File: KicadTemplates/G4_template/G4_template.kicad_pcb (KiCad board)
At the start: 2 copper layers, 71.1 x 83.2 mm, 10 parts, among them J1 Conn_01x04_Female, J2 Conn_01x03_Male, J3 Conn_01x03_Male, J4 Conn_02x10_Odd_Even, J5 Conn_02x03_Odd_Even, J6 Conn_01x01_Female, SW1 SW_SPDT, U2 NUCLEO-G491RE

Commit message: updated template
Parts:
- removed U2: NUCLEO-G491RE, G4Lib:MODULE_NUCLEO-G491RE
- added J_PWR1: Conn_01x05_Female, Connector_JST:JST_XH_S5B-XH-A_1x05_P2.50mm_Horizontal, F.Cu at (118.7, 59.1)
- added R1: 4.4K, Resistor_THT:R_Axial_DIN0207_L6.3mm_D2.5mm_P7.62mm_Horizontal, F.Cu at (153.0, 66.0)
- added R2: 4.4K, Resistor_THT:R_Axial_DIN0207_L6.3mm_D2.5mm_P7.62mm_Horizontal, F.Cu at (149.0, 66.0)
- added U1: NUCLEO-G491RE, G4Lib:MODULE_NUCLEO-G491RE20, F.Cu at (127.6, 94.0)
- moved J1 25.8 mm to (161.9, 65.4)
- moved J_GND1 25.6 mm to (144.1, 130.8)
- moved J_BUS1 23.7 mm to (156.8, 59.1)
- moved J_TRACK1 23.4 mm to (96.6, 59.1)
- moved J_POW1 23.3 mm to (96.5, 59.1)
- moved J_BUS2 23.1 mm to (138.4, 59.1)
- moved SW1 22.9 mm to (99.3, 70.7)
- moved J_SRV1 22.5 mm to (116.2, 125.1)
- moved J_SRV2 22.5 mm to (129.5, 125.1)
- renumbered J6 to J_GND1, J5 to J_POW1, J2 to J_SRV1, J3 to J_SRV2, J4 to J_TRACK1
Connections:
- net Net-(J_BUS1-Pad4) renamed CANH
- net Net-(J_BUS1-Pad5) renamed CANL
- J1 pad 1: unconnected-(J1-Pad1) -> I2C3_DTA
- J1 pad 2: unconnected-(J1-Pad2) -> I2C3_CK
- J1 pad 3: unconnected-(J1-Pad3) -> 3V3
- J1 pad 4: unconnected-(J1-Pad4) -> GND
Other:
- board size 71.1 x 83.2 mm -> 71.1 x 82.5 mm
- board text added: "Template G4 V2"
- board text added: "© Daniel Braun 2024"
- board text removed: "Template G4 V1"
- board text removed: "© Daniel Braun 2023"

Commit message: update spec
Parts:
- added R3: 4.4K, Resistor_THT:R_Axial_DIN0207_L6.3mm_D2.5mm_P7.62mm_Horizontal, F.Cu at (63.5, 101.0)
- added R4: 4.4K, Resistor_THT:R_Axial_DIN0207_L6.3mm_D2.5mm_P7.62mm_Horizontal, F.Cu at (76.2, 101.6)
- moved J_GND1 56.6 mm to (161.3, 76.8)
- moved SW1 34.9 mm to (86.4, 38.2)
- moved J_SRV1 28.6 mm to (121.9, 153.1)
- moved J_SRV2 26.6 mm to (137.1, 150.6)
- moved J_POW1 17.3 mm to (98.4, 76.2), turned to 180 degrees
- moved J_TRACK1 17.2 mm to (98.4, 76.2), turned to 180 degrees
- moved J_PWR1 6.04 mm to (116.8, 53.3)
- moved J_BUS2 5.89 mm to (137.1, 53.3)
- moved J_BUS1 5.44 mm to (156.8, 53.6)
- moved J1 1.43 mm to (161.3, 64.1)
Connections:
- J1 pad 2: I2C3_CK -> I2C3_SCL
- J_POW1 pad 6: unconnected-(J_POW1-Pin_6-Pad6) -> GND
- J_TRACK1 pad 6: unconnected-(J_TRACK1-Pin_6-Pad6) -> GND
- R2 pad 1: I2C3_CK -> I2C3_SCL
- SW1 pad 3: 5VCPU -> 5VCPU_IN
- U1 pad CN10_1: unconnected-(U1B-PC9-PadCN10_1) -> I2C3_SDA
- U1 pad CN10_11: unconnected-(U1B-PA5-PadCN10_11) -> LD2
- U1 pad CN10_12: unconnected-(U1B-PA12/CAN1TX-PadCN10_12) -> CAN_TX
- U1 pad CN10_13: unconnected-(U1B-PA6-PadCN10_13) -> ADC2_IN3
- U1 pad CN10_14: unconnected-(U1B-PA11-PadCN10_14) -> CAN_RX
- U1 pad CN10_15: unconnected-(U1B-PA7-PadCN10_15) -> ADC2_IN4
- U1 pad CN10_18: (no net) -> TIM2_CH4
- U1 pad CN10_2: unconnected-(U1B-PC8-PadCN10_2) -> I2C3_SCL
- U1 pad CN10_20: unconnected-(U1B-CN10_GND-PadCN10_20) -> GND
- U1 pad CN10_21: unconnected-(U1B-PA9-PadCN10_21) -> PWM_0_1
- U1 pad CN10_22: unconnected-(U1B-PB2-PadCN10_22) -> EECS
- U1 pad CN10_23: unconnected-(U1B-PA8-PadCN10_23) -> PWM_0_0
- U1 pad CN10_24: unconnected-(U1B-PB1-PadCN10_24) -> PWM_3_1
- U1 pad CN10_25: unconnected-(U1B-PB10-PadCN10_25) -> TIM2_CH3
- U1 pad CN10_26: unconnected-(U1B-PB15-PadCN10_26) -> SPI2_MOSI
- U1 pad CN10_28: unconnected-(U1B-PB14-PadCN10_28) -> SPI2_MISO
- U1 pad CN10_3: Net-(U1B-PB8/CAN1RX) -> unconnected-(U1B-PB8/BOOT0-PadCN10_3)
- U1 pad CN10_30: unconnected-(U1B-PB13-PadCN10_30) -> SPI2_SCK
- U1 pad CN10_31: unconnected-(U1B-PB3-PadCN10_31) -> SWO
- U1 pad CN10_33: unconnected-(U1B-PA10-PadCN10_33) -> PWM_1_0
- U1 pad CN10_34: unconnected-(U1B-PC4-PadCN10_34) -> ADC2_IN5
- U1 pad CN10_4: unconnected-(U1B-PC6-PadCN10_4) -> PWM_2_0
- U1 pad CN10_5: unconnected-(U1B-PB9-PadCN10_5) -> S_IN
- U1 pad CN10_6: unconnected-(U1B-PC5-PadCN10_6) -> ASENSE
- U1 pad CN10_9: unconnected-(U1B-CN10_GND-PadCN10_9) -> GND
- U1 pad CN7_1: unconnected-(U1A-PC10/SPI3_SCK-PadCN7_1) -> SPI3_SCK
- U1 pad CN7_13: unconnected-(U1A-PA13-PadCN7_13) -> SWDIO
- U1 pad CN7_15: unconnected-(U1A-PA14-PadCN7_15) -> SWDCLK
- U1 pad CN7_17: unconnected-(U1A-PA15-PadCN7_17) -> I2C1_SCL
- U1 pad CN7_18: unconnected-(U1A-CN7_+5V-PadCN7_18) -> 5VCPU
- U1 pad CN7_2: unconnected-(U1A-PC11/SPI3_MISO-PadCN7_2) -> S_VALID
- U1 pad CN7_21: unconnected-(U1A-PB7-PadCN7_21) -> I2C1_SDA
- U1 pad CN7_28: unconnected-(U1A-PA0-PadCN7_28) -> ADC2_IN1
- U1 pad CN7_3: unconnected-(U1A-PC12/SPI3_MOSI-PadCN7_3) -> SPI3_MOSI
- U1 pad CN7_30: unconnected-(U1A-PA1-PadCN7_30) -> ADC2_IN2
- U1 pad CN7_32: unconnected-(U1A-PA4-PadCN7_32) -> PWM_2_1
- U1 pad CN7_34: unconnected-(U1A-PB0-PadCN7_34) -> PWM_3_0
- U1 pad CN7_35: unconnected-(U1A-PC2-PadCN7_35) -> ADC2_IN8
- U1 pad CN7_36: unconnected-(U1A-PC1/PB9-PadCN7_36) -> ADC2_IN7
- U1 pad CN7_37: unconnected-(U1A-PC3-PadCN7_37) -> PWM_1_1
- U1 pad CN7_38: unconnected-(U1A-PC0/PB8-PadCN7_38) -> ADC2_IN6
- U1 pad CN7_4: unconnected-(U1A-PD2-PadCN7_4) -> S_CLR
- U1 pad CN7_5: unconnected-(U1A-VDD-PadCN7_5) -> 3V3
- U1 pad CN7_6: unconnected-(U1A-E5V-PadCN7_6) -> 5VCPU_IN
- U1 pad SER0: Net-(U1B-PB8/CAN1RX) -> unconnected-(U1-PadSER0)
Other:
- board size 71.1 x 82.5 mm -> 70.5 x 91.4 mm

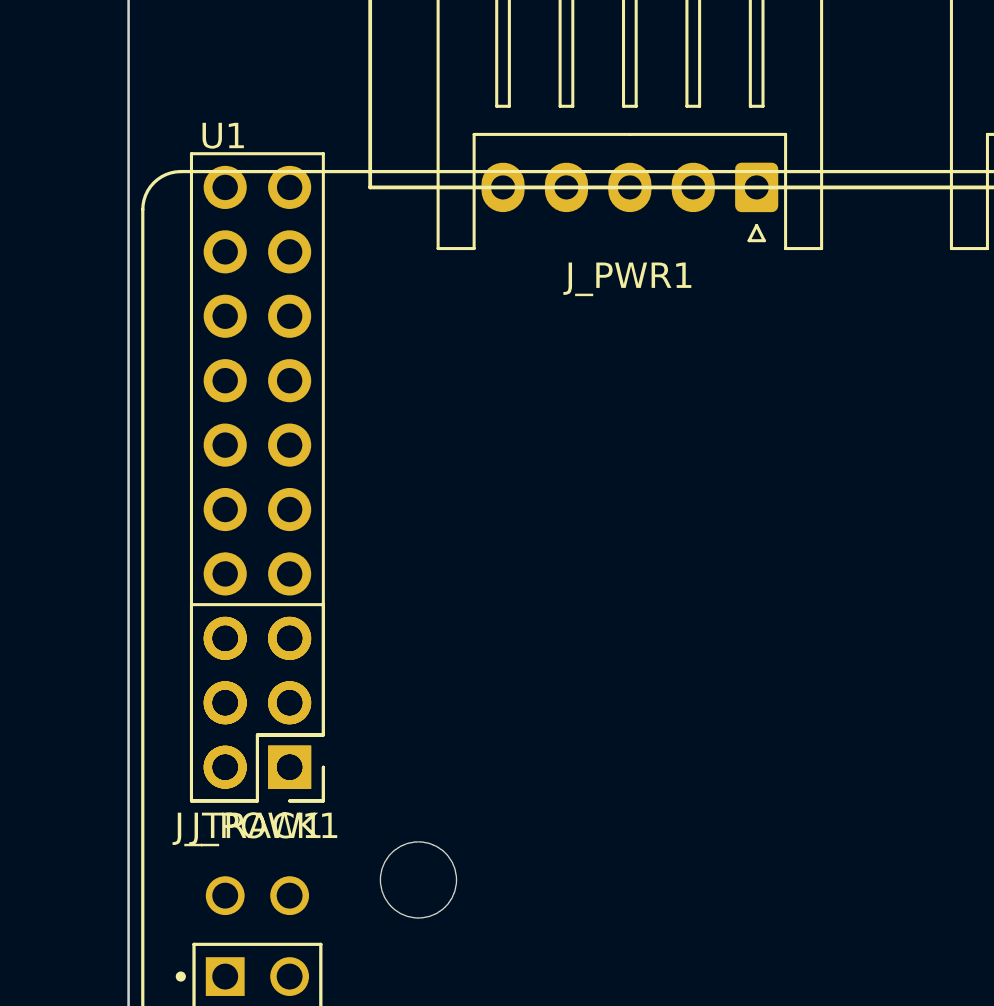
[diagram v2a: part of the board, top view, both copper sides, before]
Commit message: update spec J_TRACK and mapping
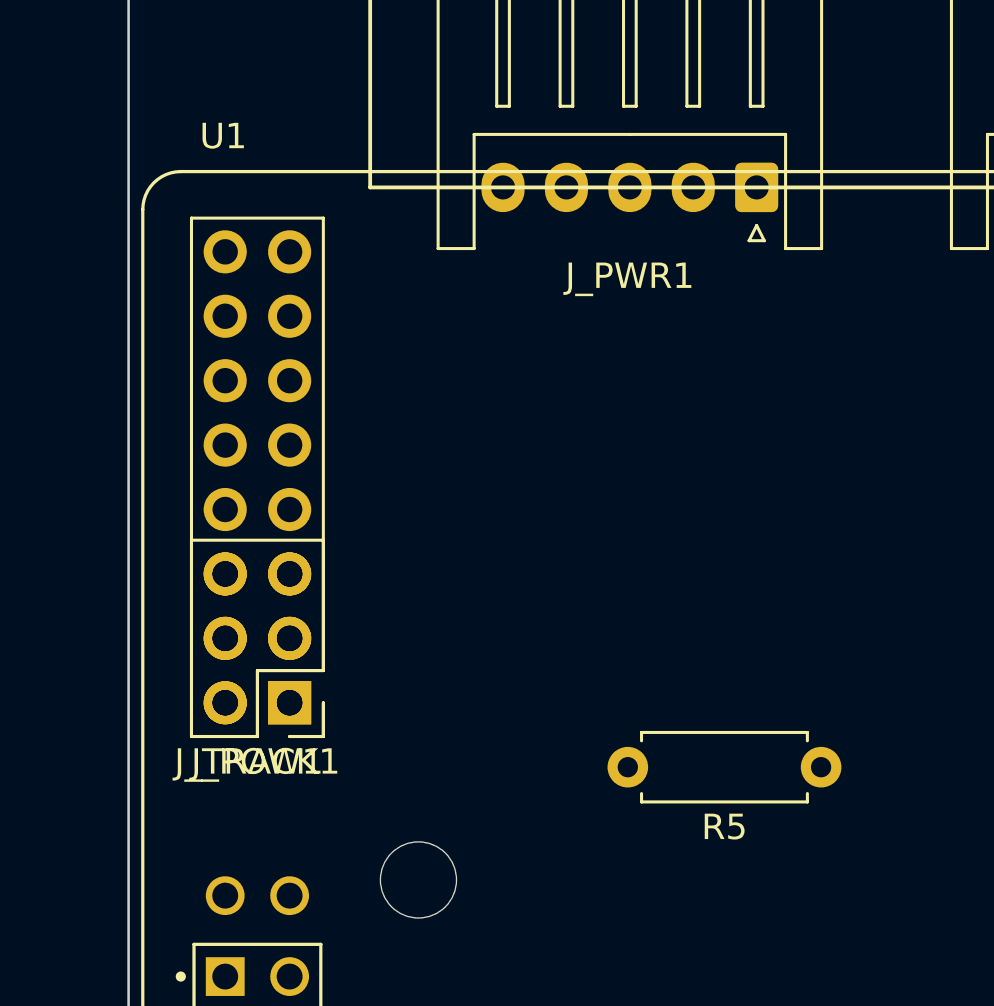
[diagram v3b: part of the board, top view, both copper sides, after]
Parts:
- added R5: 20K, Resistor_THT:R_Axial_DIN0207_L6.3mm_D2.5mm_P7.62mm_Horizontal, F.Cu at (119.4, 76.2)
- J_TRACK1: value Conn_02x10_Odd_Even -> Conn_02x08_Odd_Even; footprint Connector_PinHeader_2.54mm:PinHeader_2x10_P2.54mm_Vertical -> Connector_PinHeader_2.54mm:PinHeader_2x08_P2.54mm_Vertical
- moved J_POW1 2.54 mm to (98.4, 73.7)
- moved J_TRACK1 2.54 mm to (98.4, 73.7)
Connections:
- net R0A renamed C1B
- net R0B renamed C3B
- net RIA renamed T00A
- net RIB renamed T10A
- net T0B renamed T30A
- net T1A renamed C0A
- net T1B renamed C2A
- net T2A renamed C0B
- net T2B renamed C2B
- net T3A renamed C1A
- net T3B renamed C3A
- J_POW1 pad 6: GND -> unconnected-(J_POW1-Pin_6-Pad6)
- J_TRACK1 pad 6: GND -> T20A
- J_TRACK1 pad 7: T0A -> unconnected-(J_TRACK1-Pin_7-Pad7)
- U1 pad SER3: unconnected-(U1-PadSER3) -> S_IN

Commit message: update spec POW_CTRL
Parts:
- added JP1: SolderJumper_2_Open, Jumper:SolderJumper-2_P1.3mm_Open_Pad1.0x1.5mm, F.Cu at (183.7, 62.8)
- added JP2: SolderJumper_2_Open, Jumper:SolderJumper-2_P1.3mm_Open_Pad1.0x1.5mm, F.Cu at (183.7, 66.3)
- added JP3: SolderJumper_2_Open, Jumper:SolderJumper-2_P1.3mm_Open_Pad1.0x1.5mm, F.Cu at (183.7, 69.8)
- added JP4: SolderJumper_2_Open, Jumper:SolderJumper-2_P1.3mm_Open_Pad1.0x1.5mm, F.Cu at (188.0, 62.8)
- added JP5: SolderJumper_2_Open, Jumper:SolderJumper-2_P1.3mm_Open_Pad1.0x1.5mm, F.Cu at (188.0, 66.3)
- added JP6: SolderJumper_2_Open, Jumper:SolderJumper-2_P1.3mm_Open_Pad1.0x1.5mm, F.Cu at (188.0, 69.8)
- added JP7: SolderJumper_2_Open, Jumper:SolderJumper-2_P1.3mm_Open_Pad1.0x1.5mm, F.Cu at (192.4, 62.8)
- added JP8: SolderJumper_2_Open, Jumper:SolderJumper-2_P1.3mm_Open_Pad1.0x1.5mm, F.Cu at (192.4, 66.3)
- added JP9: SolderJumper_2_Open, Jumper:SolderJumper-2_P1.3mm_Open_Pad1.0x1.5mm, F.Cu at (192.4, 69.8)
- added R_IDENT1: ~, Resistor_THT:R_Axial_DIN0207_L6.3mm_D2.5mm_P7.62mm_Horizontal, F.Cu at (194.1, 90.4)
- added U3: 74HC594, Package_DIP:DIP-16_W7.62mm_LongPads, F.Cu at (182.9, 86.4)
- J_PWR1: footprint Connector_JST:JST_XH_S5B-XH-A_1x05_P2.50mm_Horizontal -> Connector_JST:JST_XH_S4B-XH-A-1_1x04_P2.50mm_Horizontal
- moved R5 75.4 mm to (194.1, 86.3), turned to 0 degrees
- moved J_PWR1 1.27 mm to (116.8, 52.1)
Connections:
- J_PWR1 pad 4: unconnected-(J_PWR1-Pin_4-Pad4) -> POW_CTRL
- U1 pad CN10_27: unconnected-(U1B-PB4-PadCN10_27) -> POW_CTRL
- U1 pad CN10_5: S_IN -> SER3
- U1 pad SER3: S_IN -> unconnected-(U1-PadSER3)

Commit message: updated template
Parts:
- added J_AGND1: Conn_01x01_Female, Connector_PinHeader_2.54mm:PinHeader_1x01_P2.54mm_Vertical, F.Cu at (149.9, 61.0)
- JP1, JP2, JP3, JP4, JP5, JP6, JP7, JP8, JP9: value SolderJumper_2_Open -> Jumper_2_Open; footprint Jumper:SolderJumper-2_P1.3mm_Open_Pad1.0x1.5mm -> Connector_PinHeader_2.54mm:PinHeader_1x02_P2.54mm_Vertical
- moved JP9 19.5 mm to (210.8, 63.5)
- moved JP8 14.1 mm to (206.2, 63.5)
- moved JP6 10.9 mm to (196.9, 63.5)
- moved JP1 10.1 mm to (173.6, 63.5)
- moved JP7 9.16 mm to (201.5, 63.5)
- moved JP3 6.40 mm to (182.9, 63.5)
- moved JP2 6.10 mm to (178.3, 63.5)
- moved JP5 5.03 mm to (192.2, 63.5)
- moved JP4 0.89 mm to (187.6, 63.5)
- renumbered R_IDENT1 to R_ID1
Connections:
- JP1 pad 1: SPI3_MOSI -> unconnected-(JP1-A-Pad1)
- JP2 pad 1: SER0 -> unconnected-(JP2-A-Pad1)
- JP3 pad 1: SER1 -> unconnected-(JP3-A-Pad1)
- JP4 pad 1: SER2 -> unconnected-(JP4-A-Pad1)
- JP5 pad 1: SER3 -> unconnected-(JP5-A-Pad1)
- U3 pad 11: SPI3_CLK -> SPI3_SCK
